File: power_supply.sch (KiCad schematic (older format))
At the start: 32 parts, among them U1 LM2575S-5.0_NOPB, U2 LM2575S-5.0_NOPB, U3 LD1117S33TR_SOT223, U4 LD1117S33TR_SOT223

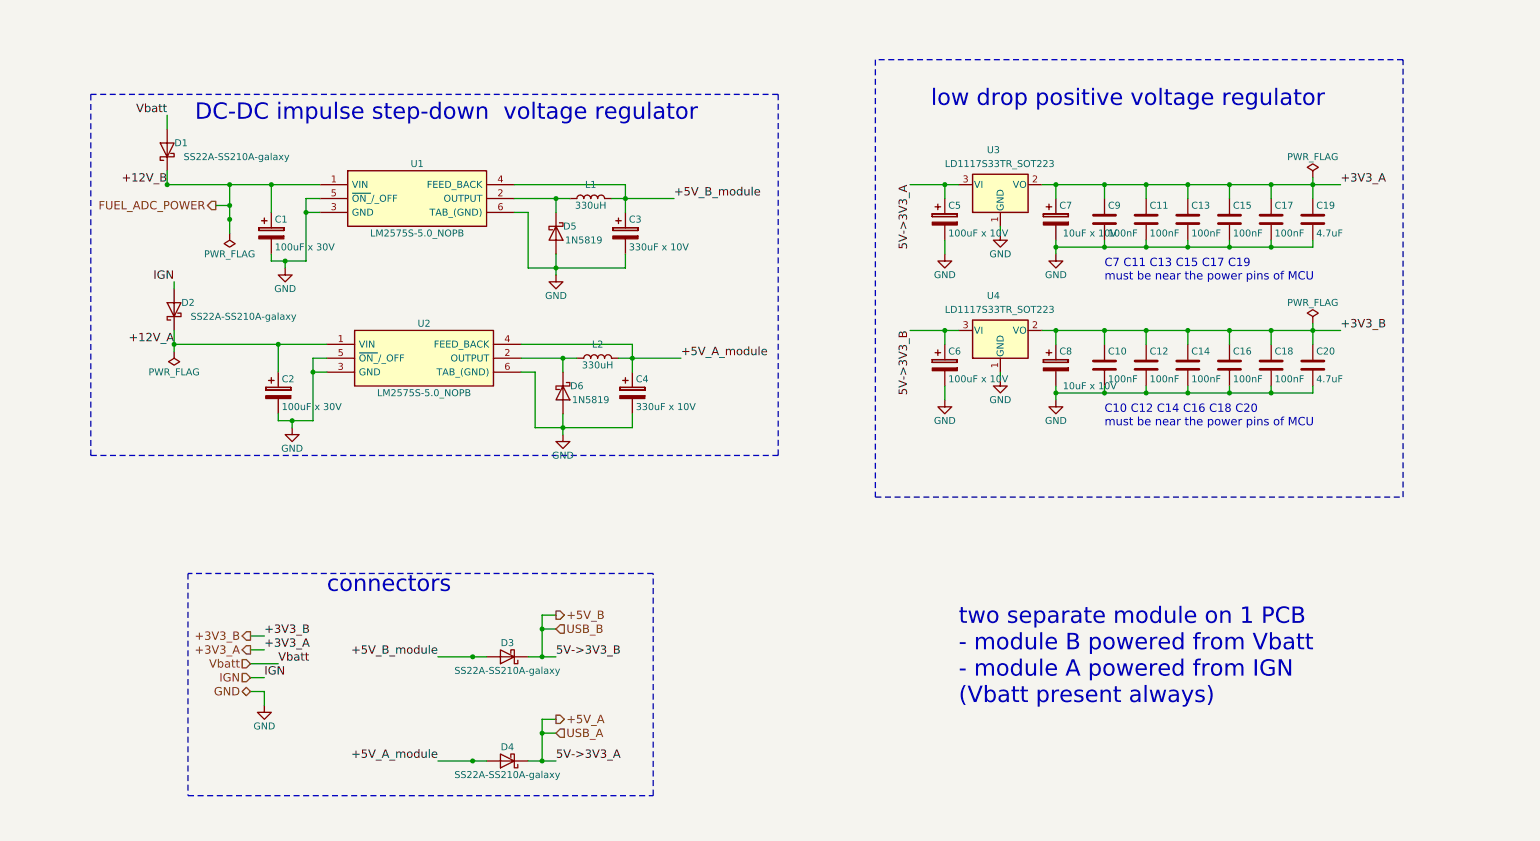
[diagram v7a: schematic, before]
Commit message: redone shematic of power supply, fix usb_vbus and swd diods connections, change mcu capacitors connections
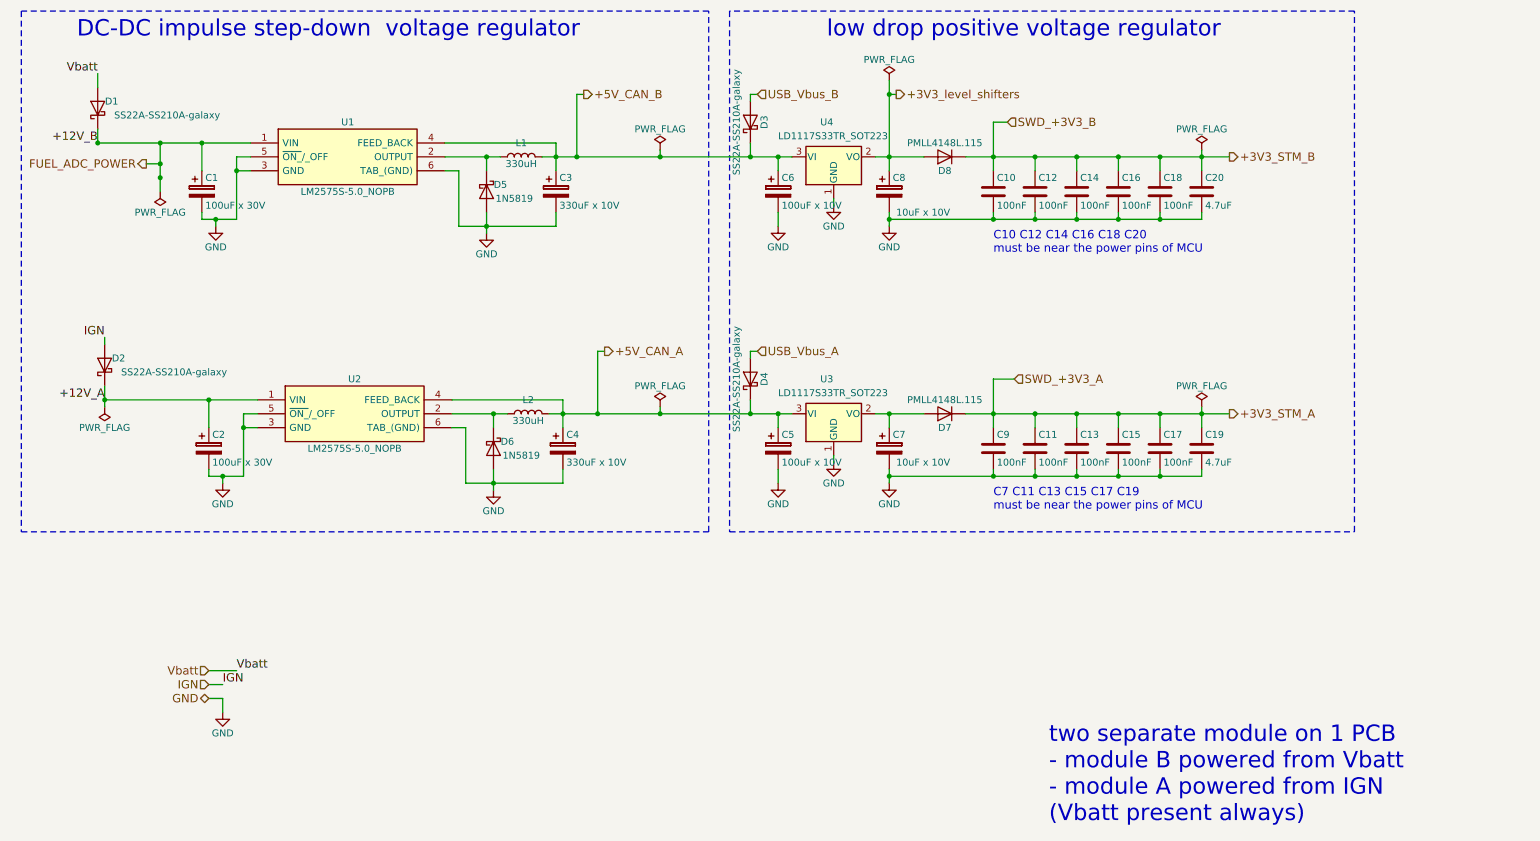
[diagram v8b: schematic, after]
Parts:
- added D7, D8: PMLL4148L.115, Diodes_SMD:D_SC-80, symbol D
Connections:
- net +3V3_A renamed +3V3_STM_A
- net +3V3_STM_A: now also D7.1 (K); no longer C7.1, U3.2 (VO)
- net +3V3_B renamed +3V3_STM_B
- net +3V3_STM_B: now also D8.1 (K); no longer C8.1, U4.2 (VO)
- net +5V_A renamed +5V_CAN_A
- net +5V_CAN_A: now also C4.1, L2.2, U2.4 (FEED_BACK)
- removed net +5V_A_module: C4.1, D4.2 (A), L2.2, U2.4 (FEED_BACK)
- net +5V_B renamed +5V_CAN_B
- net +5V_CAN_B: now also C3.1, L1.2, U1.4 (FEED_BACK)
- removed net +5V_B_module: C3.1, D3.2 (A), L1.2, U1.4 (FEED_BACK)
- new net: C7.1, D7.2 (A), U3.2 (VO)
- new net +3V3_level_shifters: C8.1, D8.2 (A), U4.2 (VO)
- new net USB_Vbus_A: D4.2 (A)
- new net USB_Vbus_B: D3.2 (A)
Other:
- note removed: "connectors"
- moved on the sheet: C1, C10, C11, C12, C13, C14, C15, C16, C17, C18, C19, C2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
